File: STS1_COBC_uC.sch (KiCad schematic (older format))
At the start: 76 parts, among them IC1 STM32F411RET6TR, IC2 STWD100PYW83F, J1 Conn_01x01_Male, J10 Conn_01x01_Male, J11 Conn_01x01_Male, J12 Conn_01x01_Male, J13 Conn_01x01_Male, J14 Conn_01x01_Male, J15 Conn_01x01_Male, J16 Conn_01x01_Male, J17 Conn_01x01_Male, J18 Conn_01x01_Male, J19 Conn_01x01_Male, J2 Conn_01x05_Female, J20 Conn_01x01_Male, J21 Conn_01x01_Male, J22 Conn_01x01_Male, J23 Conn_01x01_Male, J24 Conn_01x01_Male, J25 Conn_01x01_Male, J26 Conn_01x01_Male, J27 Conn_01x01_Male, J28 Conn_01x01_Male, J29 Conn_01x01_Male, J3 Conn_01x01_Male, J30 Conn_01x01_Male, J31 Conn_01x01_Male, J32 Conn_01x01_Male, J33 Conn_01x01_Male, J34 Conn_01x01_Male, J35 Conn_01x01_Male, J36 Conn_01x01_Male, J37 Conn_01x01_Male, J38 Conn_01x01_Male, J4 Conn_01x01_Male, J41 Conn_01x01_Male, J42 Conn_01x01_Male, J43 Conn_01x01_Male, J44 Conn_01x01_Male, J45 Conn_01x01_Male, J46 Conn_01x01_Male, J47 Conn_01x01_Male, J48 Conn_01x01_Male, J49 Conn_01x01_Male, J5 Conn_01x01_Male, J50 Conn_01x01_Male, J51 Conn_01x01_Male, J52 Conn_01x01_Male, J53 Conn_01x01_Male, J6 Conn_01x01_Male, J7 Conn_01x01_Male, J8 Conn_01x01_Male, J9 Conn_01x01_Male, Y1 12MHz

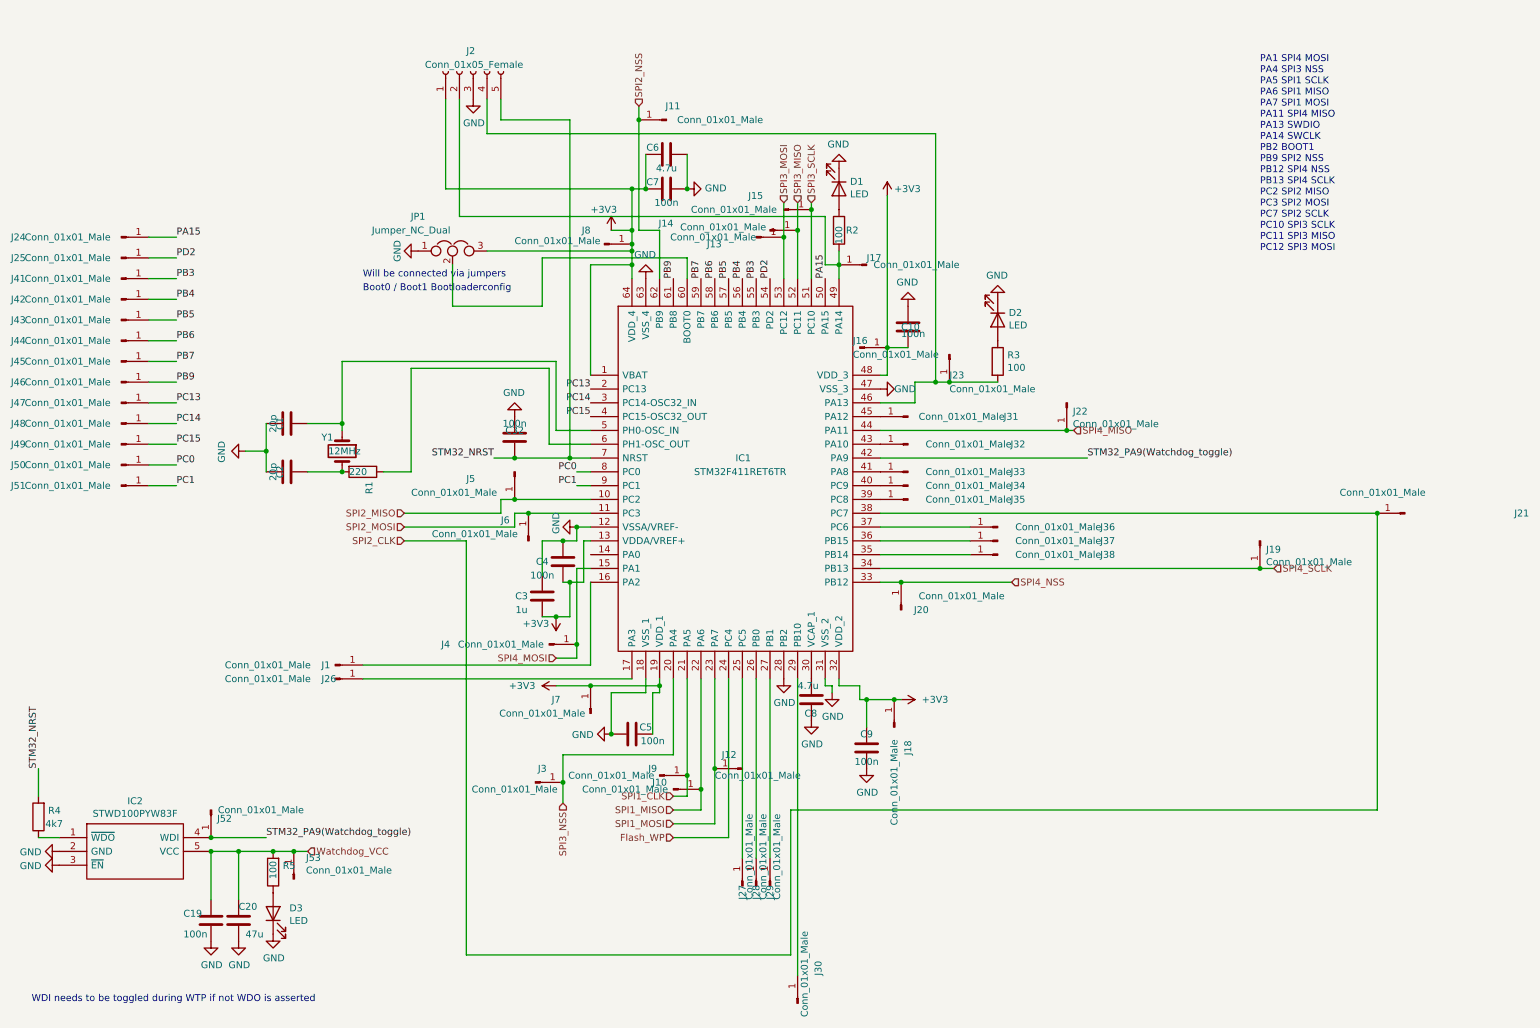
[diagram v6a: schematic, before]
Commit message: component layout finished -> now wiring
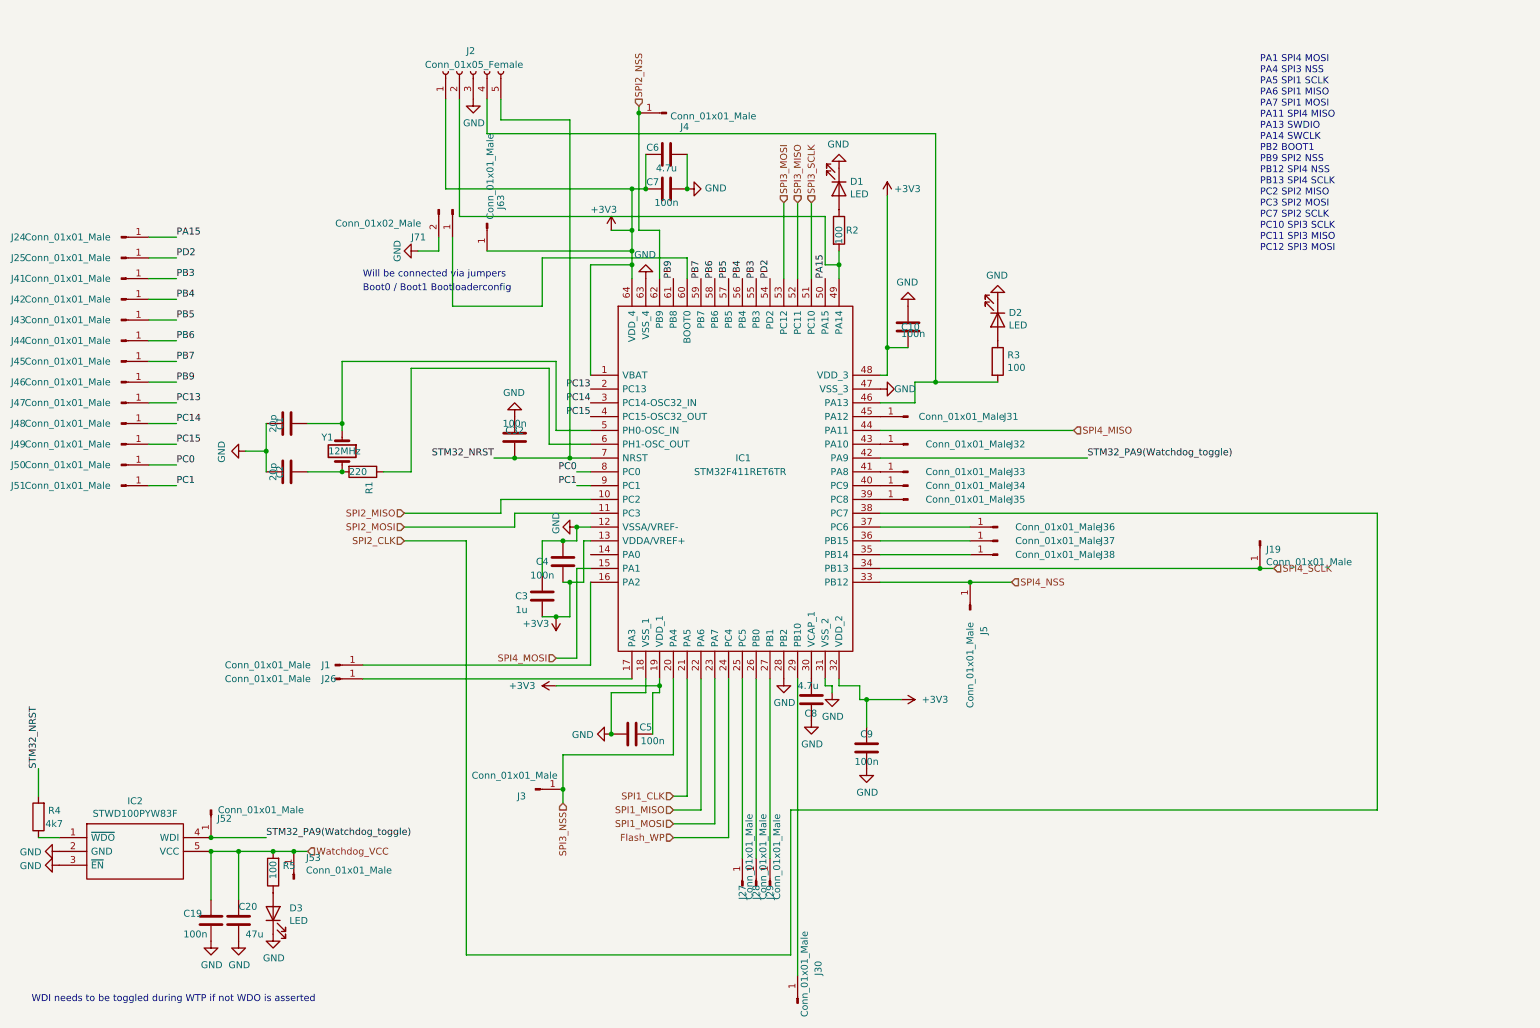
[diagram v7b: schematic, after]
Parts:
- removed J10, J11, J12, J13, J14, J15, J16, J17, J18, J20, J21, J22, J23, J6, J7, J8, J9: Conn_01x01_Male, Connector_PinHeader_2.54mm:PinHeader_1x01_P2.54mm_Vertical, symbol Connector:Conn_01x01_Male
- removed JP1: Jumper_NC_Dual, Connector_PinHeader_2.54mm:PinHeader_1x03_P2.54mm_Vertical, symbol Device:Jumper_NC_Dual
- added J63: Conn_01x01_Male, Connector_PinHeader_2.54mm:PinHeader_1x01_P2.54mm_Vertical, symbol Connector:Conn_01x01_Male
- added J71: Conn_01x02_Male, Connector_PinHeader_2.54mm:PinHeader_1x02_P2.54mm_Vertical, symbol Connector:Conn_01x02_Male
- Y1: footprint (none) -> Crystal:Crystal_SMD_5032-2Pin_5.0x3.2mm_HandSoldering
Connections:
- net +3V3: now also J63.1 (Pin_1)
- net GND: now also J71.2 (Pin_2)
- net SPI2_MISO: no longer J5.1 (Pin_1)
- net SPI2_NSS: now also J4.1 (Pin_1)
- net SPI4_MOSI: no longer J4.1 (Pin_1)
- net SPI4_NSS: now also J5.1 (Pin_1)
- net at IC1.60 (BOOT0): now also J71.1 (Pin_1)
